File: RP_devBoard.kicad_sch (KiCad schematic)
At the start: 0 parts

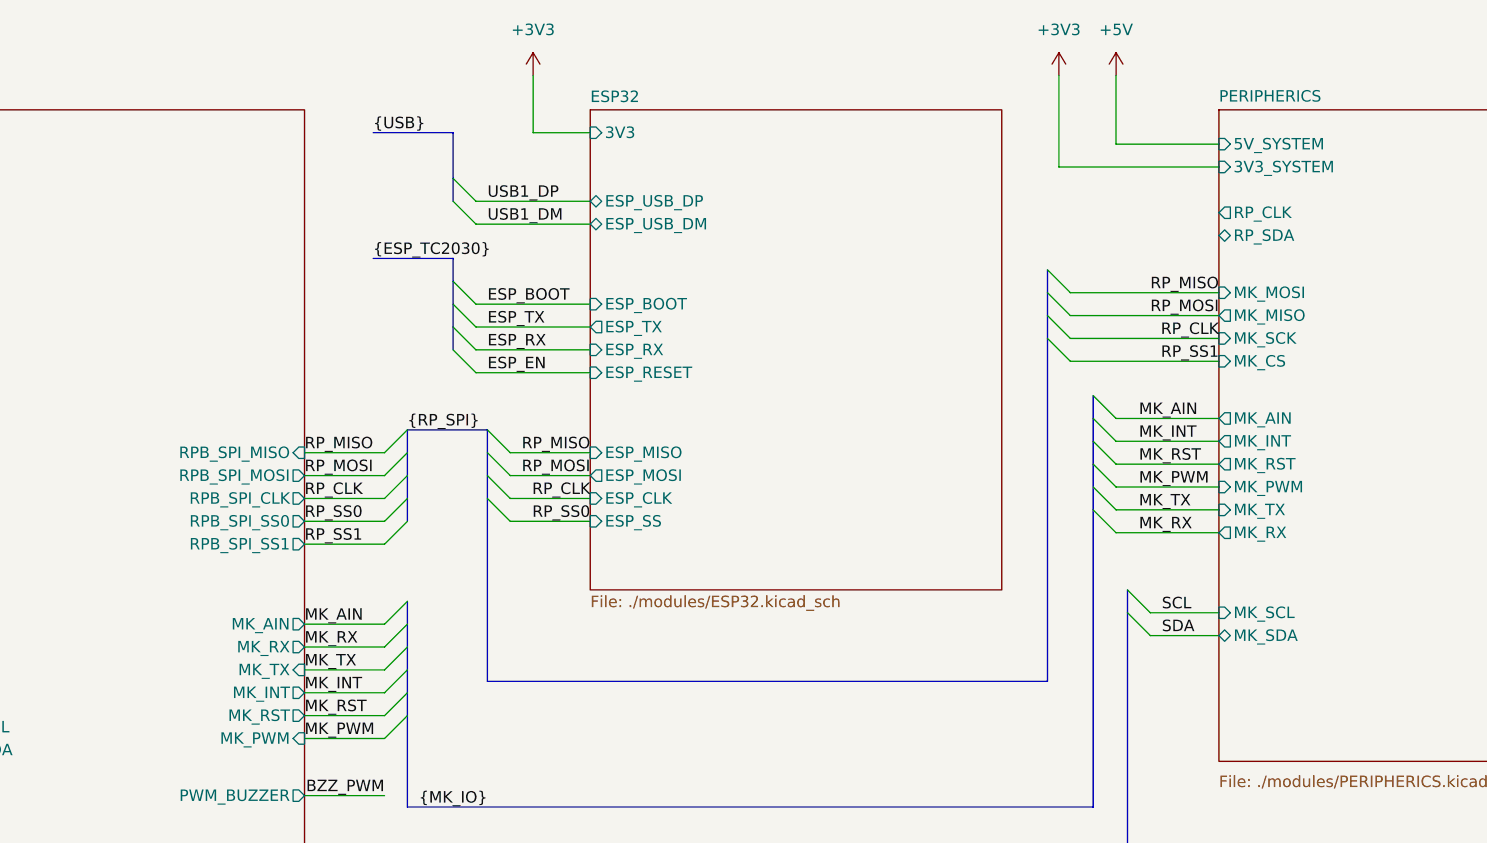
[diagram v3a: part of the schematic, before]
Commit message: correction of mikroBUS, USB on ESP32 and power mosfet
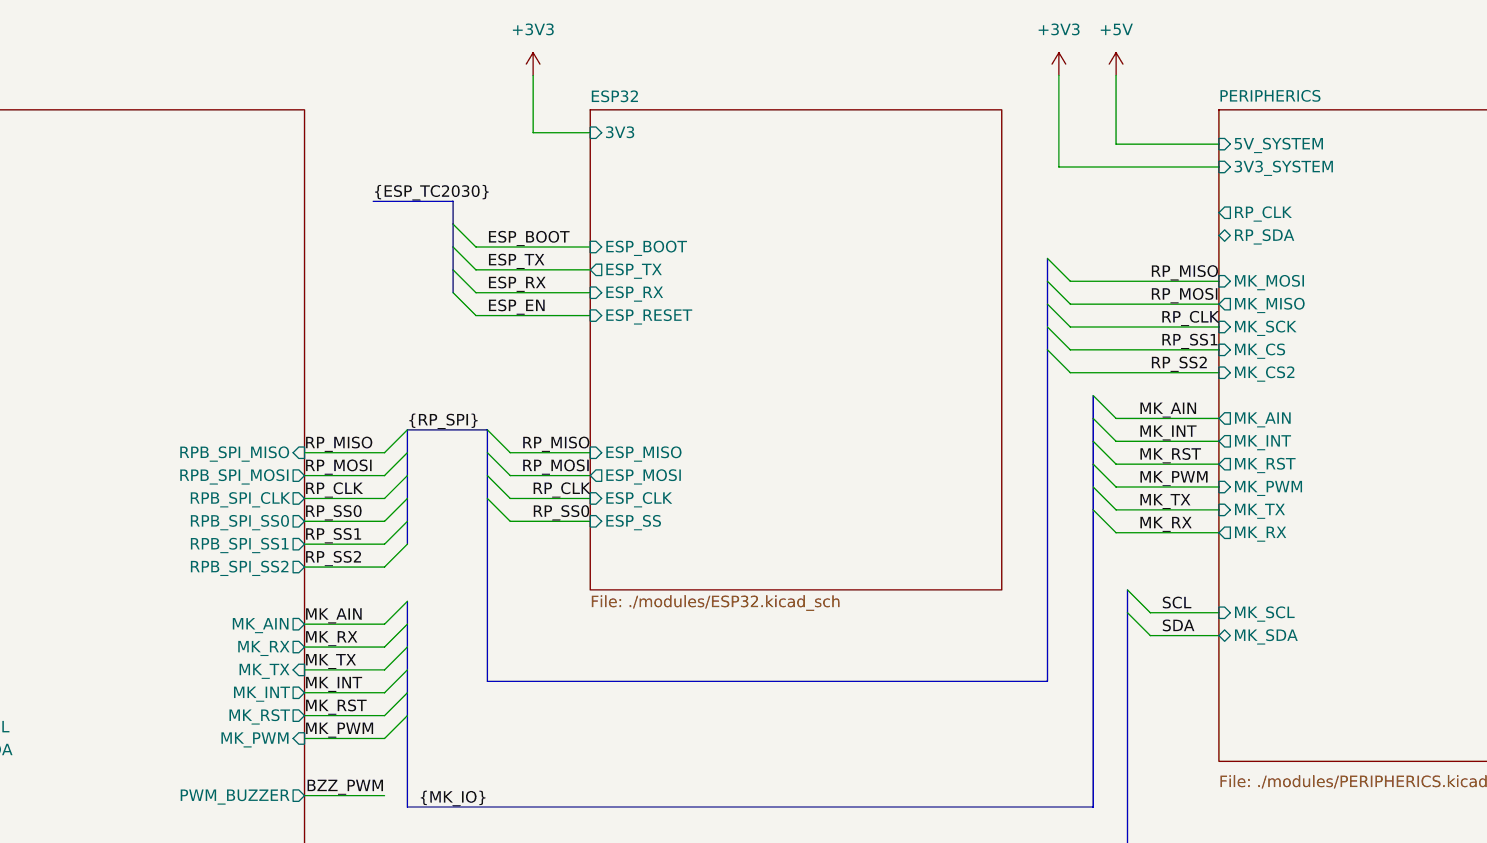
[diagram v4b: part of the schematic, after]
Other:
- sheet ESP32 ports: added none; removed ESP_USB_DM, ESP_USB_DP
- sheet PERIPHERICS ports: added MK_CS2; removed none
- sheet RP2350B ports: added RPB_SPI_SS2; removed none

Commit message: save
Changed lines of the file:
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@@
+	)
+	(bus_entry
+		(at 237.49 54.61)
+		(size 2.54 2.54)
+		(stroke
+			(width 0)
+			(type default)
+		)
 	)
 	(bus_entry
@@
 	)
 	(bus_entry
+		(at 237.49 57.15)
+		(size 2.54 2.54)
+		(stroke
+			(width 0)
+			(type default)
+		)
+	)
+	(bus_entry
 		(at 86.36 64.77)
 		(size 2.54 2.54)
@@
 		)
 	)
+	(bus
+		(pts
+			(xy 231.14 54.61) (xy 237.49 54.61)
+		)
+		(stroke
+			(width 0)
+			(type default)
+		)
+	)
 	(wire
 		(pts
@@
 	(bus
 		(pts
+			(xy 237.49 54.61) (xy 237.49 57.15)
+		)
+		(stroke
+			(width 0)
+			(type default)
+		)
+	)
+	(bus
+		(pts
 			(xy 238.76 130.81) (xy 238.76 133.35)
 		)
@@
 		)
 	)
+	(wire
+		(pts
+			(xy 240.03 59.69) (xy 248.92 59.69)
+		)
+		(stroke
+			(width 0)
+			(type default)
+		)
+	)
 	(bus
 		(pts
@@
 		(pts
 			(xy 241.3 133.35) (xy 248.92 133.35)
+		)
+		(stroke
+			(width 0)
+			(type default)
+		)
+	)
+	(wire
+		(pts
+			(xy 240.03 57.15) (xy 248.92 57.15)
 		)
 		(stroke
@@
 		)
 	)
+	(label "{I2C}"
+		(at 231.14 54.61 0)
+		(effects
+			(font
+				(size 1.27 1.27)
+			)
+			(justify left bottom)
+		)
+	)
 	(label "RP_SWD"
 		(at 88.9 69.85 0)
@@
 		)
 	)
+	(label "SDA"
+		(at 240.03 59.69 0)
+		(effects
+			(font
+				(size 1.27 1.27)
+			)
+			(justify left bottom)
+		)
+	)
 	(label "RP_MISO"
 		(at 248.92 64.77 180)
@@
 		(effects
 			(font
+				(size 1.27 1.27)
+			)
+			(justify left bottom)
+		)
+	)
+	(label "SCL"
+		(at 240.03 57.15 0)
+		(effects
+			(font

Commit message: Cambio de layout, correccion de pinout
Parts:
- added H1, H2, H3, H4: MountingHole, MountingHole:MountingHole_3.2mm_M3, symbol Mechanical:MountingHole
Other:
- sheet PERIPHERICS ports: added MK_AIN2, MK_CS1, MK_INT2, MK_PWM2, MK_RST2, MK_RX2, MK_TX2; removed MK_CS, RP_CLK, RP_SDA
- sheet RP2350B ports: added MK_AIN2, MK_INT2, MK_PWM2, MK_RST2, MK_RX2, MK_TX2; removed none

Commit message: finishing version 1.0
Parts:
- H1, H2, H3, H4: footprint MountingHole:MountingHole_3.2mm_M3 -> MountingHole:MountingHole_3.2mm_M3_DIN965_Pad
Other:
- sheet RP2350B ports: added none; removed RPB_SWO
- sheet TC2030_PORTS ports: added none; removed RP_SWO
- title: (none) -> ${PROJECT}
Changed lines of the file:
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@@
 	(generator_version "9.0")
 	(paper "A4")
+	(title_block
+		(title "${PROJECT}")
+		(date "2026-03-08")
+		(rev "${VERSION}")
+	)
 	(bus_alias "ESP_TC2030"
 		(members "ESP_BOOT" "ESP_TX" "ESP_RX" "ESP_EN")
@@
 	)
 	(bus_alias "RP_TC2030"
-		(members "RP_NRESET" "RP_SWO" "RP_SWD" "RP_SWCLK")
+		(members "RP_NRESET" "RP_SWD" "RP_SWCLK")
 	)
 	(bus_alias "USB"
@@
 	)
 	(bus_entry
-		(at 67.31 96.52)
+		(at 67.31 93.98)
 		(size -2.54 2.54)
 		(stroke
@@
 	)
 	(bus_entry
-		(at 87.63 55.88)
-		(size 2.54 2.54)
-		(stroke
-			(width 0)
-			(type default)
-		)
-	)
-	(bus_entry
 		(at 67.31 107.95)
 		(size -2.54 2.54)
@@
 	)
 	(bus_entry
-		(at 87.63 58.42)
+		(at 87.63 55.88)
 		(size 2.54 2.54)
 		(stroke
@@
 	)
 	(bus_entry
-		(at 87.63 60.96)
+		(at 87.63 58.42)
 		(size 2.54 2.54)
 		(stroke
@@
 	)
 	(bus_entry
-		(at 67.31 99.06)
-		(size -2.54 2.54)
-		(stroke
-			(width 0)
-			(type default)
-		)
-	)
-	(bus_entry
-		(at 67.31 93.98)
+		(at 67.31 96.52)
 		(size -2.54 2.54)
 		(stroke
@@
 	(bus
 		(pts
-			(xy 87.63 60.96) (xy 87.63 90.17)
+			(xy 87.63 58.42) (xy 87.63 90.17)
 		)
 		(stroke
@@
 		)
 	)
-	(bus
-		(pts
-			(xy 67.31 93.98) (xy 67.31 96.52)
-		)
-		(stroke
-			(width 0)
-			(type default)
-		)
-	)
 	(wire
 		(pts
@@
 	(bus
 		(pts
-			(xy 67.31 96.52) (xy 67.31 99.06)
+			(xy 67.31 93.98) (xy 67.31 96.52)
 		)
 		(stroke
@@
 		)
 	)
-	(wire
-		(pts
-			(xy 54.61 96.52) (xy 64.77 96.52)
-		)
-		(stroke
-			(width 0)
-			(type default)
-		)
-	)
 	(bus
 		(pts
@@
 	(wire
 		(pts
-			(xy 160.02 107.95) (xy 158.75 107.95)
-		)
-		(stroke
-			(width 0)
-			(type default)
-		)
-	)
-	(wire
-		(pts
 			(xy 54.61 113.03) (xy 64.77 113.03)
 		)
@@
 		)
 	)
-	(bus
-		(pts
-			(xy 87.63 53.34) (xy 87.63 55.88)
-		)
-		(stroke
-			(width 0)
-			(type default)
-		)
-	)
 	(wire
 		(pts
@@
 	(wire
 		(pts
-			(xy 90.17 63.5) (xy 102.87 63.5)
+			(xy 90.17 60.96) (xy 102.87 60.96)
 		)
 		(stroke
@@
 	(bus
 		(pts
-			(xy 87.63 55.88) (xy 87.63 58.42)
+			(xy 87.63 53.34) (xy 87.63 55.88)
 		)
 		(stroke
@@
 	(wire
 		(pts
-			(xy 54.61 99.06) (xy 64.77 99.06)
+			(xy 54.61 96.52) (xy 64.77 96.52)
 		)
 		(stroke
@@
 	(bus
 		(pts
-			(xy 87.63 58.42) (xy 87.63 60.96)
+			(xy 87.63 55.88) (xy 87.63 58.42)
 		)
 		(stroke
@@
 	(wire
 		(pts
-			(xy 54.61 101.6) (xy 64.77 101.6)
+			(xy 54.61 99.06) (xy 64.77 99.06)
 		)
 		(stroke
@@
 	(wire
 		(pts
-			(xy 90.17 58.42) (xy 102.87 58.42)
-		)
-		(stroke
-			(width 0)
-			(type default)
-		)
-	)
-	(wire
-		(pts
 			(xy 148.59 121.92) (xy 165.1 121.92)
 		)
@@
 	(wire
 		(pts
-			(xy 90.17 60.96) (xy 102.87 60.96)
+			(xy 90.17 58.42) (xy 102.87 58.42)
 		)
 		(stroke
@@
 	)
 	(label "RP_SWD"
-		(at 54.61 99.06 0)
+		(at 54.61 96.52 0)
 		(effects
 			(font
@@
 	)
 	(label "RP_SWD"
-		(at 90.17 60.96 0)
-		(effects
-			(font
-				(size 1.27 1.27)
-			)
-			(justify left bottom)
-		)
-	)
-	(label "RP_SWO"
-		(at 54.61 96.52 0)
+		(at 90.17 58.42 0)
 		(effects
 			(font
@@
 		)
 	)
-	(label "RP_SWO"
-		(at 90.17 58.42 0)
-		(effects
-			(font
-				(size 1.27 1.27)
-			)
-			(justify left bottom)
-		)
-	)
 	(label "RP_MOSI"
 		(at 186.69 45.72 180)
@@
 	)
 	(label "RP_SWCLK"
-		(at 90.17 63.5 0)
+		(at 90.17 60.96 0)
 		(effects
 			(font
@@
 	)
 	(label "RP_SWCLK"
-		(at 54.61 101.6 0)
+		(at 54.61 99.06 0)
 		(effects
 			(font
@@
 			)
 		)
-		(property "Footprint" "MountingHole:MountingHole_3.2mm_M3"
+		(property "Footprint" "MountingHole:MountingHole_3.2mm_M3_DIN965_Pad"
 			(at 148.59 185.42 0)
 			(effects
@@
 			)
 		)
-		(property "Footprint" "MountingHole:MountingHole_3.2mm_M3"
+		(property "Footprint" "MountingHole:MountingHole_3.2mm_M3_DIN965_Pad"
 			(at 125.73 185.42 0)
 			(effects
@@
 			)
 		)
-		(property "Footprint" "MountingHole:MountingHole_3.2mm_M3"
+		(property "Footprint" "MountingHole:MountingHole_3.2mm_M3_DIN965_Pad"
 			(at 148.59 177.8 0)
 			(effects
@@
 			)
 		)
-		(property "Footprint" "MountingHole:MountingHole_3.2mm_M3"
+		(property "Footprint" "MountingHole:MountingHole_3.2mm_M3_DIN965_Pad"
 			(at 125.73 177.8 0)
 			(effects
@@
 		)
 		(pin "RP_SWCLK" input
-			(at 102.87 63.5 180)
-			(effects
-				(font
-					(size 1.27 1.27)
-				)
-				(justify left)
-			)
-		)
-		(pin "RPB_SWO" output
-			(at 102.87 58.42 180)
+			(at 102.87 60.96 180)
 			(effects
 				(font
@@
 		)
 		(pin "RP_SWD" bidirectional
-			(at 102.87 60.96 180)
+			(at 102.87 58.42 180)
 			(effects
 				(font
@@
 			)
 		)
-		(pin "RP_SWO" output
-			(at 54.61 96.52 0)
-			(effects
-				(font
-					(size 1.27 1.27)
-				)
-				(justify right)
-			)
-		)
 		(pin "RP_SWD" bidirectional
-			(at 54.61 99.06 0)
+			(at 54.61 96.52 0)
 			(effects
 				(font
@@
 		)
 		(pin "RP_SWCLK" output
-			(at 54.61 101.6 0)
+			(at 54.61 99.06 0)
 			(effects
 				(font
